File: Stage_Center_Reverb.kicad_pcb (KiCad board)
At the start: 2 copper layers, 75 x 50 mm, 43 parts, among them J10 Power, J2 Output, J3 Tank, SW2 kill, U1 TL072, U10 L78L15, U11 L79L15, U2 TL072

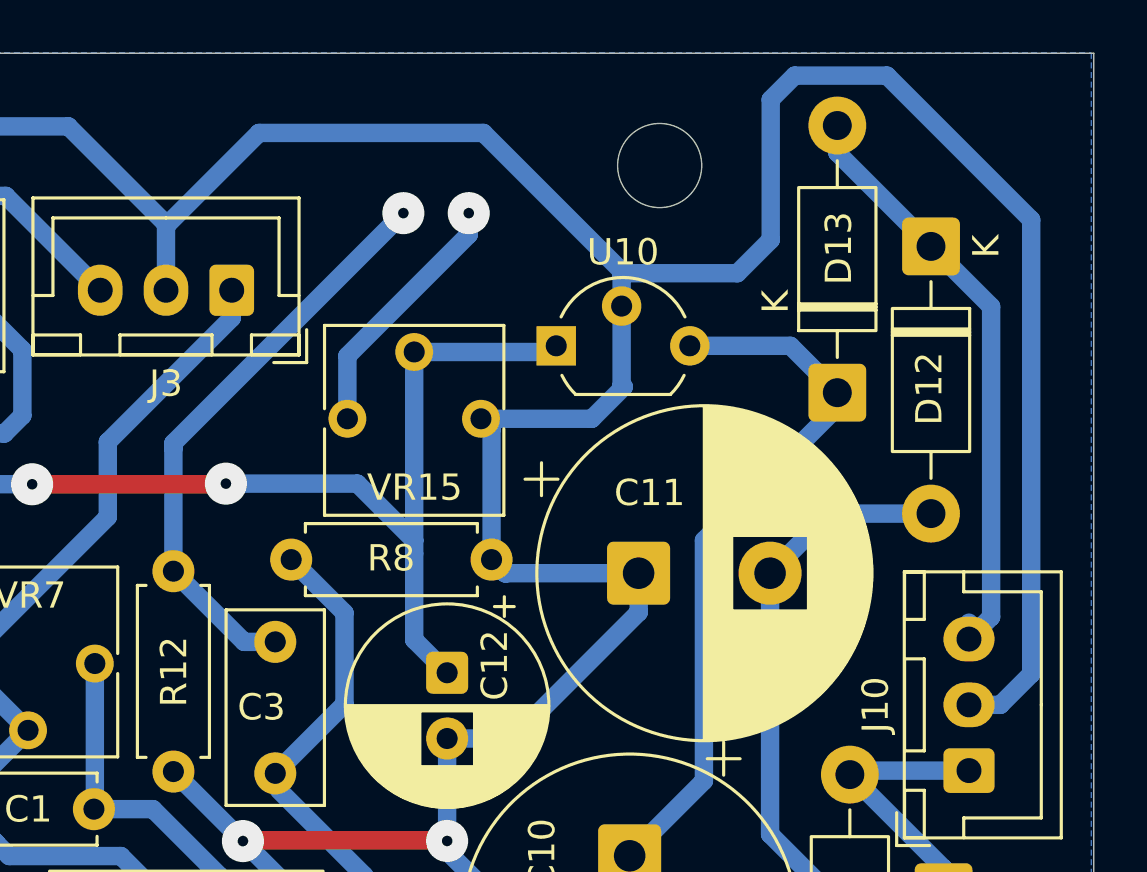
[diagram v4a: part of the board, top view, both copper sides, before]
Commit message: LED周りの修正
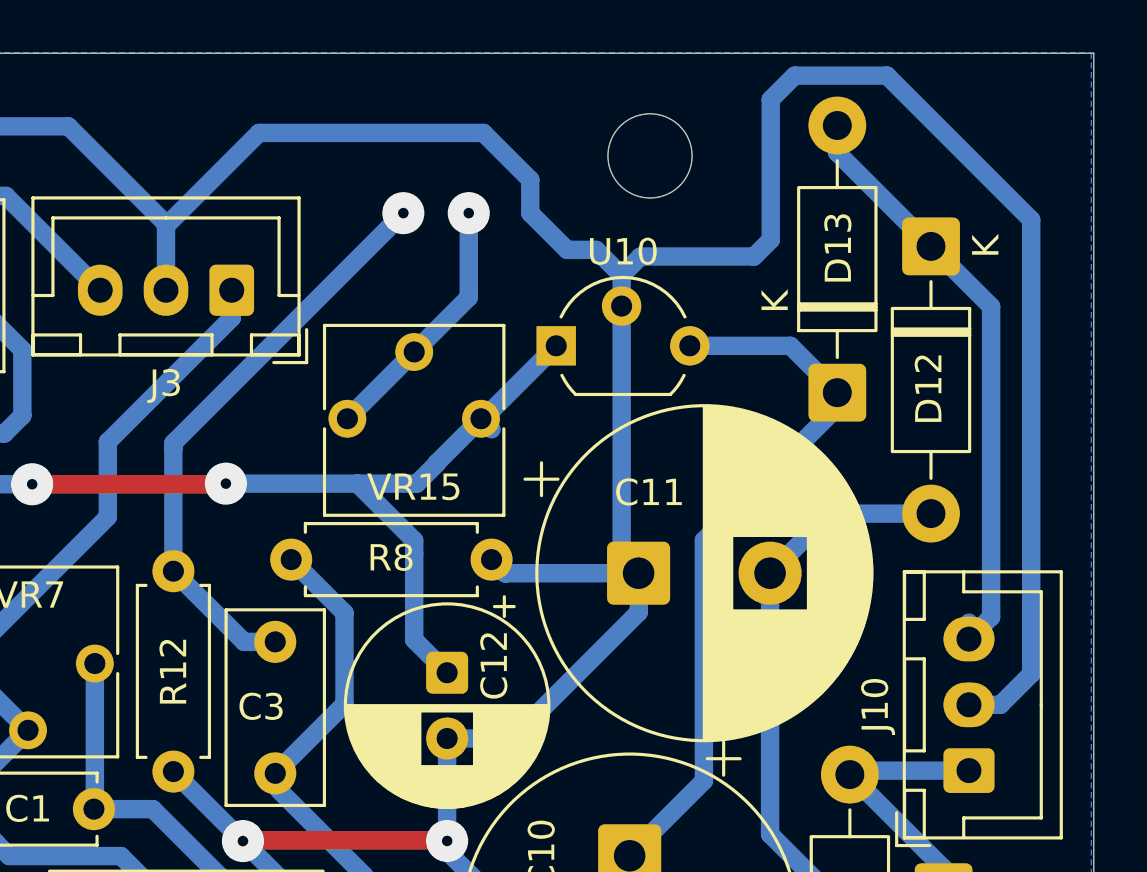
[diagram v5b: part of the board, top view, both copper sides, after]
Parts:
- moved H2 0.52 mm to (151.6, 80.4)
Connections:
- VR15 pad 1: GNDPWR -> +15V
- VR15 pad 2: +15V -> Net-(D1-A)
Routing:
- net GNDPWR: track 259.6 -> 256.1 mm
- net +15V: track 78.4 -> 76.0 mm
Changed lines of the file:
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@@
 			(layers "*.Cu" "*.Mask")
 			(remove_unused_layers no)
-			(net 2 "GNDPWR")
+			(net 11 "+15V")
 			(pinfunction "1")
 			(pintype "passive")
@@
 			(layers "*.Cu" "*.Mask")
 			(remove_unused_layers no)
-			(net 11 "+15V")
+			(net 10 "Net-(D1-A)")
 			(pinfunction "2")
 			(pintype "passive")
@@
 	(footprint "MountingHole:MountingHole_3.2mm_M3"
 		(layer "F.Cu")
-		(at 151.987032 80.740322)
+		(at 151.619702 80.37336)
 		(descr "Mounting Hole 3.2mm, M3, no annular, generated by kicad-footprint-generator mountinghole.py")
 		(tags "mountinghole M3")
@@
 	)
 	(segment
+		(start 150.540715 84.917285)
+		(end 151.257 84.201)
+		(width 0.7)
+		(layer "B.Cu")
+		(net 2)
+	)
+	(segment
+		(start 148.463 83.947)
+		(end 147.066 82.55)
+		(width 0.7)
+		(layer "B.Cu")
+		(net 2)
+	)
+	(segment
 		(start 149.075225 111.991225)
 		(end 143.904379 106.820379)
@@
 	)
 	(segment
+		(start 155.575 84.201)
+		(end 156.21 83.566)
+		(width 0.7)
+		(layer "B.Cu")
+		(net 2)
+	)
+	(segment
 		(start 133.25 83)
 		(end 133.212379 83.037621)
@@
 	)
 	(segment
-		(start 133.25 83)
-		(end 136.75 79.5)
+		(start 147.066 82.55)
+		(end 147.066 81.28)
 		(width 0.7)
 		(layer "B.Cu")
@@
 	)
 	(segment
-		(start 136.75 79.5)
-		(end 145.286 79.5)
+		(start 150.540715 86.085317)
+		(end 150.540715 95.598838)
 		(width 0.7)
 		(layer "B.Cu")
@@
 	)
 	(segment
-		(start 156.21 78.232)
-		(end 156.21 83.566)
-		(width 0.7)
-		(layer "B.Cu")
-		(net 2)
-	)
-	(segment
 		(start 114.26974 104.67826)
 		(end 114.26974 106.403176)
@@
 	)
 	(segment
-		(start 150.482785 116.587128)
-		(end 150.817726 116.922069)
-		(width 0.7)
-		(layer "B.Cu")
-		(net 2)
-	)
-	(segment
-		(start 163.75 101.25)
-		(end 163.25 101.25)
+		(start 145.286 79.5)
+		(end 136.75 79.5)
 		(width 0.7)
 		(layer "B.Cu")
@@
 	)
 	(segment
-		(start 145.593282 90.772289)
-		(end 145.191522 90.370529)
+		(start 150.482785 116.587128)
+		(end 150.817726 116.922069)
 		(width 0.7)
 		(layer "B.Cu")
@@
 	)
 	(segment
-		(start 145.593282 95.726533)
-		(end 145.593282 90.772289)
+		(start 163.75 101.25)
+		(end 163.25 101.25)
 		(width 0.7)
 		(layer "B.Cu")
@@
 	)
 	(segment
-		(start 145.286 79.5)
-		(end 150.622 84.836)
-		(width 0.7)
-		(layer "B.Cu")
-		(net 2)
-	)
-	(segment
 		(start 104.394 95.972809)
 		(end 104.394 98.044)
@@
 	)
 	(segment
-		(start 150.540715 86.085317)
-		(end 150.540715 89.072715)
-		(width 0.7)
-		(layer "B.Cu")
-		(net 2)
-	)
-	(segment
-		(start 150.622 84.836)
-		(end 150.540715 84.917285)
-		(width 0.7)
-		(layer "B.Cu")
-		(net 2)
-	)
-	(segment
-		(start 149.405471 90.370529)
-		(end 145.191522 90.370529)
-		(width 0.7)
-		(layer "B.Cu")
-		(net 2)
-	)
-	(segment
 		(start 146.110051 96.243302)
 		(end 145.593282 95.726533)
@@
 	)
 	(segment
-		(start 150.622 89.154)
-		(end 149.405471 90.370529)
-		(width 0.7)
-		(layer "B.Cu")
-		(net 2)
-	)
-	(segment
-		(start 160.632917 77.320917)
-		(end 157.121083 77.320917)
+		(start 143.904379 106.4)
+		(end 143.904379 106.426)
 		(width 0.7)
 		(layer "B.Cu")
@@
 	)
 	(segment
-		(start 143.904379 106.4)
-		(end 143.904379 106.426)
+		(start 117.959215 79.25)
+		(end 118 79.25)
 		(width 0.7)
 		(layer "B.Cu")
@@
 	)
 	(segment
-		(start 156.21 83.566)
-		(end 154.94 84.836)
+		(start 129.5 79.25)
+		(end 133.25 83)
 		(width 0.7)
 		(layer "B.Cu")
@@
 	)
 	(segment
-		(start 117.959215 79.25)
-		(end 118 79.25)
+		(start 104.394 98.044)
+		(end 102.87 99.568)
 		(width 0.7)
 		(layer "B.Cu")
@@
 	)
 	(segment
-		(start 166.116 82.804)
-		(end 160.632917 77.320917)
+		(start 113.796912 112.995681)
+		(end 111.795681 112.995681)
 		(width 0.7)
 		(layer "B.Cu")
@@
 	)
 	(segment
-		(start 129.5 79.25)
-		(end 133.25 83)
+		(start 151.257 84.201)
+		(end 155.575 84.201)
 		(width 0.7)
 		(layer "B.Cu")
@@
 	)
 	(segment
-		(start 104.394 98.044)
-		(end 102.87 99.568)
+		(start 99.270621 98.298)
+		(end 99.270621 96.828825)
 		(width 0.7)
 		(layer "B.Cu")
@@
 	)
 	(segment
-		(start 113.796912 112.995681)
-		(end 111.795681 112.995681)
+		(start 156.21 83.566)
+		(end 156.21 78.232)
 		(width 0.7)
 		(layer "B.Cu")
@@
 	)
 	(segment
-		(start 99.270621 98.298)
-		(end 99.270621 96.828825)
+		(start 150.540715 95.598838)
+		(end 151.185179 96.243302)
 		(width 0.7)
 		(layer "B.Cu")
@@
 	)
 	(segment
-		(start 166.116 100.076)
-		(end 166.116 82.804)
+		(start 136.75 79.5)
+		(end 133.25 83)
 		(width 0.7)
 		(layer "B.Cu")
@@
 	)
 	(segment
+		(start 150.540715 86.085317)
+		(end 150.540715 84.917285)
+		(width 0.7)
+		(layer "B.Cu")
+		(net 2)
+	)
+	(segment
 		(start 144.2491 116.587128)
 		(end 150.482785 116.587128)
@@
 	)
 	(segment
-		(start 150.540715 84.917285)
-		(end 150.540715 86.085317)
+		(start 147.066 81.28)
+		(end 145.286 79.5)
 		(width 0.7)
 		(layer "B.Cu")
@@
 	)
 	(segment
-		(start 100.478 111.4)
-		(end 96.52 107.442)
+		(start 149.57043 83.947)
+		(end 148.463 83.947)
 		(width 0.7)
 		(layer "B.Cu")
@@
 	(segment
 		(start 157.121083 77.320917)
-		(end 156.21 78.232)
+		(end 160.632917 77.320917)
 		(width 0.7)
 		(layer "B.Cu")
@@
 	)
 	(segment
-		(start 163.75 101.25)
-		(end 164.942 101.25)
+		(start 100.478 111.4)
+		(end 96.52 107.442)
 		(width 0.7)
 		(layer "B.Cu")
@@
 	)
 	(segment
-		(start 143.904379 102.529885)
-		(end 146.390115 102.529885)
+		(start 160.632917 77.320917)
+		(end 166.116 82.804)
 		(width 0.7)
 		(layer "B.Cu")
@@
 	)
 	(segment
-		(start 150.540715 89.072715)
-		(end 150.622 89.154)
+		(start 166.116 100.076)
+		(end 164.942 101.25)
+		(width 0.7)
+		(layer "B.Cu")
+		(net 2)
+	)
+	(segment
+		(start 143.904379 102.529885)
+		(end 146.390115 102.529885)
 		(width 0.7)
 		(layer "B.Cu")
@@
 	)
 	(segment
+		(start 166.116 82.804)
+		(end 166.116 100.076)
+		(width 0.7)
+		(layer "B.Cu")
+		(net 2)
+	)
+	(segment
 		(start 133.212379 83.037621)
 		(end 133.212379 85.482834)
@@
 	)
 	(segment
+		(start 150.540715 84.917285)
+		(end 149.57043 83.947)
+		(width 0.7)
+		(layer "B.Cu")
+		(net 2)
+	)
+	(segment
 		(start 102.87 99.568)
 		(end 100.076 99.568)
@@
 	(segment
 		(start 164.942 101.25)
-		(end 166.116 100.076)
+		(end 163.75 101.25)
 		(width 0.7)
 		(layer "B.Cu")
@@
 	)
 	(segment
-		(start 154.94 84.836)
-		(end 150.622 84.836)
+		(start 156.21 78.232)
+		(end 157.121083 77.320917)
 		(width 0.7)
 		(layer "B.Cu")
@@
 	)
 	(segment
-		(start 140.111522 87.980478)
-		(end 144.726988 83.365012)
+		(start 140.111522 90.370529)
+		(end 142.651522 87.830529)
 		(width 0.7)
 		(layer "B.Cu")
@@
 	)
 	(segment
-		(start 144.726988 83.365012)
-		(end 144.726988 82.55)
+		(start 144.726988 85.755063)
+		(end 142.651522 87.830529)
 		(width 0.7)
 		(layer "B.Cu")
@@
 	)
 	(segment
-		(start 140.111522 90.370529)
-		(end 140.111522 87.980478)
+		(start 144.726988 82.55)
+		(end 144.726988 85.755063)
 		(width 0.7)
 		(layer "B.Cu")
@@
 	)
 	(segment
+		(start 143.51 92.052051)
+		(end 143.51 92.075)
+		(width 0.7)
+		(layer "B.Cu")
+		(net 11)
+	)
+	(segment
 		(start 142.651522 94.996)
 		(end 142.651522 95.5)
@@
 	)
 	(segment
-		(start 147.818836 87.830529)
-		(end 148.053034 87.596331)
+		(start 145.191522 90.370529)
+		(end 145.278836 90.370529)
 		(width 0.7)
 		(layer "B.Cu")
@@
 	)
 	(segment
+		(start 145.593282 90.772289)
+		(end 145.191522 90.370529)
+		(width 0.7)
+		(layer "B.Cu")
+		(net 11)
+	)
+	(segment
 		(start 125.854058 94.109942)
 		(end 125.854058 92.860269)
@@
 	)
 	(segment
+		(start 143.51 92.052051)
+		(end 145.191522 90.370529)
+		(width 0.7)
+		(layer "B.Cu")
+		(net 11)
+	)
+	(segment
+		(start 140.492522 92.837)
+		(end 142.748 92.837)
+		(width 0.7)
+		(layer "B.Cu")
+		(net 11)
+	)
+	(segment
+		(start 140.4924 92.836878)
+		(end 140.492522 92.837)
+		(width 0.7)
+		(layer "B.Cu")
+		(net 11)
+	)
+	(segment
 		(start 142.651522 98.777028)
 		(end 143.904379 100.029885)
@@
 	)
 	(segment
-		(start 142.651522 87.830529)
-		(end 147.818836 87.830529)
+		(start 145.278836 90.370529)
+		(end 148.053034 87.596331)
+		(width 0.7)
+		(layer "B.Cu")
+		(net 11)
+	)
+	(segment
+		(start 143.51 92.075)
+		(end 142.748 92.837)
 		(width 0.7)
 		(layer "B.Cu")
@@
 		(width 0.7)
 		(layer "B.Cu")
-		(net 11)
-	)
-	(segment
-		(start 142.651522 87.830529)
-		(end 142.651522 94.996)
-		(width 0.7)
-		(layer "B.Cu")

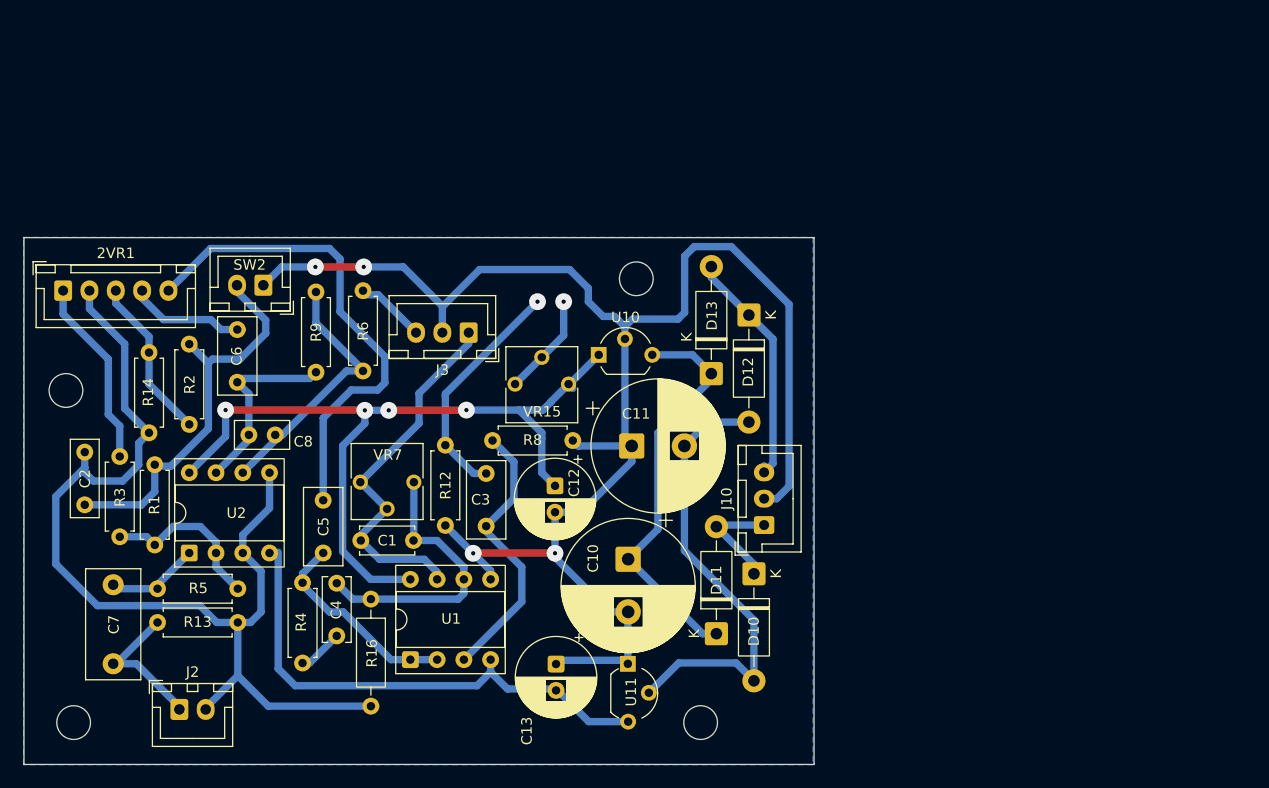
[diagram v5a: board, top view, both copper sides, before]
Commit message: 配置換えしたときにGNDの接続が抜けていた
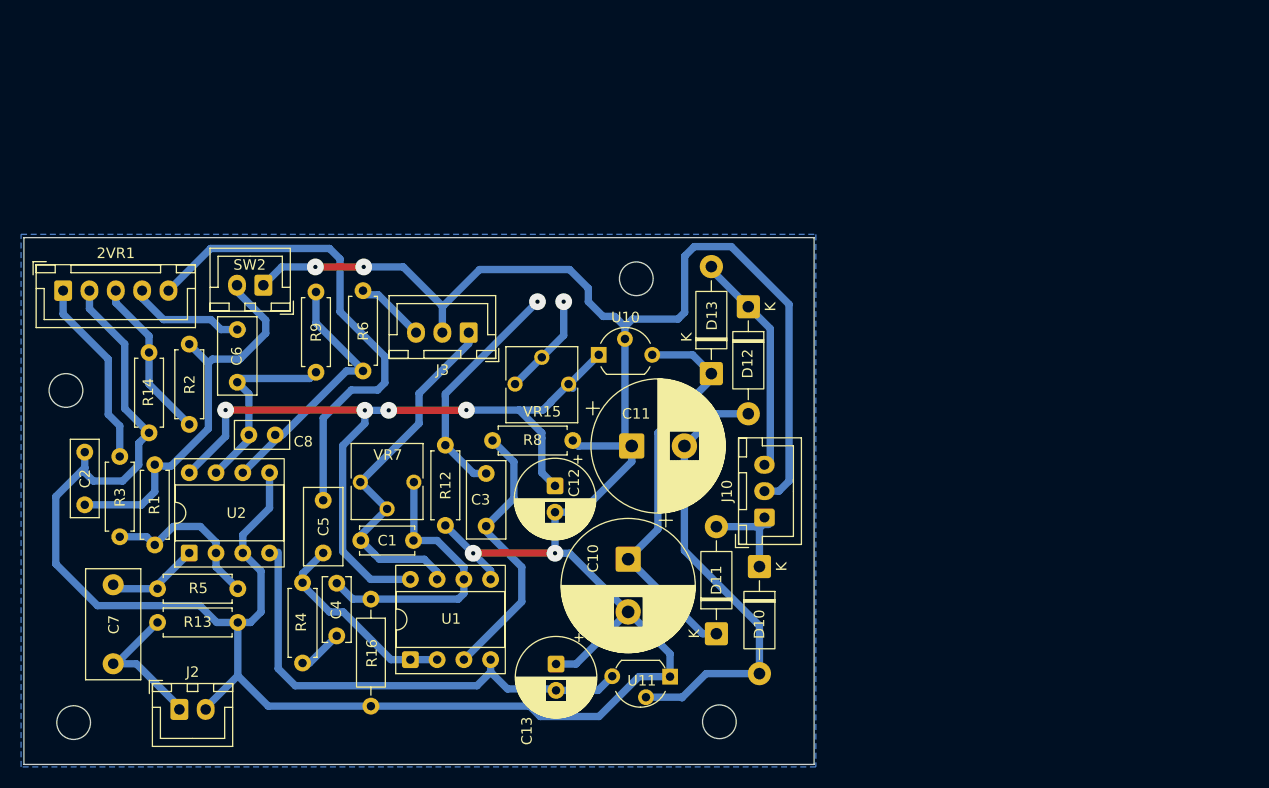
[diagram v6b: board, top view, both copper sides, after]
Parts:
- moved U11 3.73 mm to (154.6, 118.4), turned to 180 degrees
- moved H4 1.78 mm to (159.5, 122.4)
- moved D10 0.86 mm to (163.3, 107.7)
- moved D12 0.79 mm to (162.3, 83.0)
- moved J10 0.72 mm to (163.8, 103.0)
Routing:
- net GNDPWR: track 256.1 -> 290.2 mm
- net -15V: track 48.6 -> 46.4 mm
- net Net-(D12-K): track 23.4 -> 21.4 mm
- net Net-(D10-K): track 12.2 -> 10.5 mm

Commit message: C4,R6のハイパスフィルタのカットオフ周波数をを下げた
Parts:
- C4: value 1000pF -> 1500pF
- R16: value 330k -> 560k
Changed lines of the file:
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@@
 			)
 		)
-		(property "Value" "330k"
+		(property "Value" "560k"
 			(at 5.08 2.37 270)
 			(layer "F.Fab")
@@
 			)
 		)
-		(property "Value" "1000pF"
+		(property "Value" "1500pF"
 			(at 2.5 2.5 90)
 			(layer "F.Fab")
